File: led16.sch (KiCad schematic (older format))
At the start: 32 parts

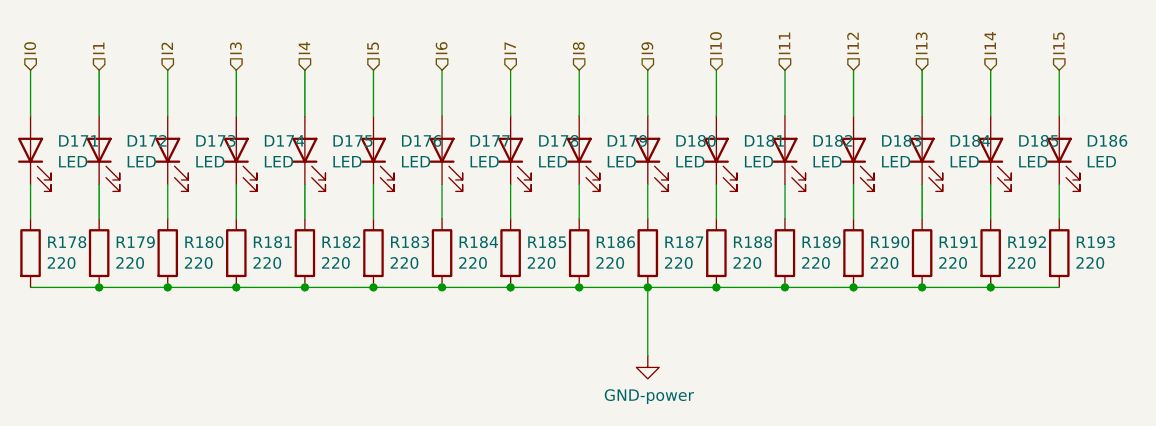
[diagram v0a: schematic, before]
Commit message: added display
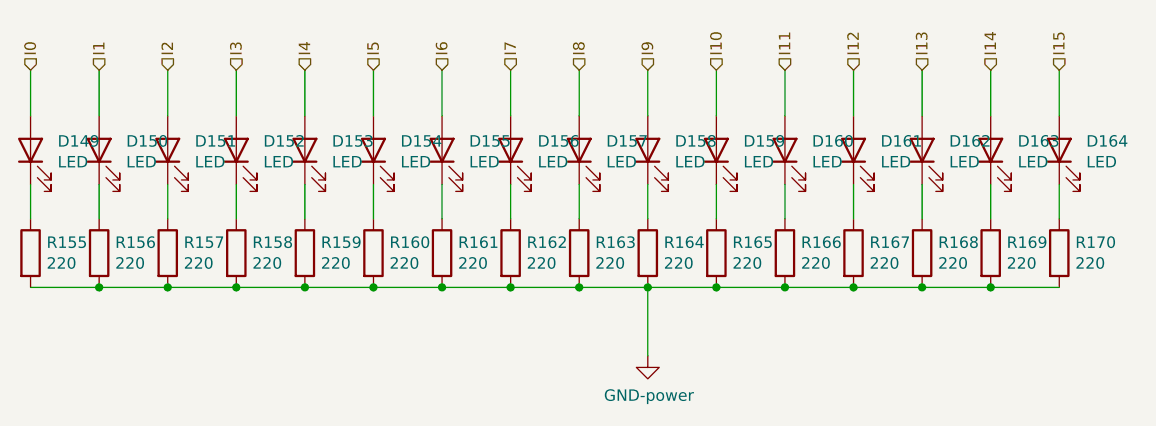
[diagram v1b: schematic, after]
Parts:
- renumbered D155 to D133, D156 to D134, D157 to D135, D158 to D136, D159 to D137, D160 to D138, D161 to D139, D162 to D140, D163 to D141, D164 to D142, D165 to D143, D166 to D144, D167 to D145, D168 to D146, D169 to D147, D170 to D148, R162 to R139, R163 to R140, R164 to R141, R165 to R142, R166 to R143, R167 to R144, R168 to R145, R169 to R146, R170 to R147, R171 to R148, R172 to R149, R173 to R150, R174 to R151, R175 to R152, R176 to R153, R177 to R154
